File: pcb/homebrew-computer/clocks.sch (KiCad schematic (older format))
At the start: 6 parts

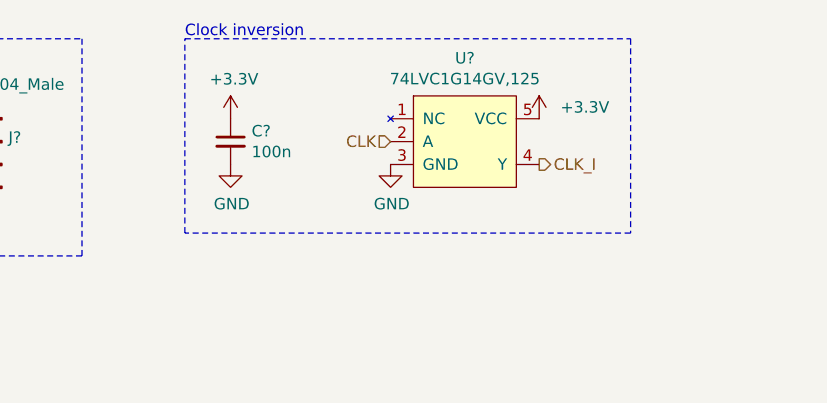
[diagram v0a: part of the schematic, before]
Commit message: Add the memory interface logic
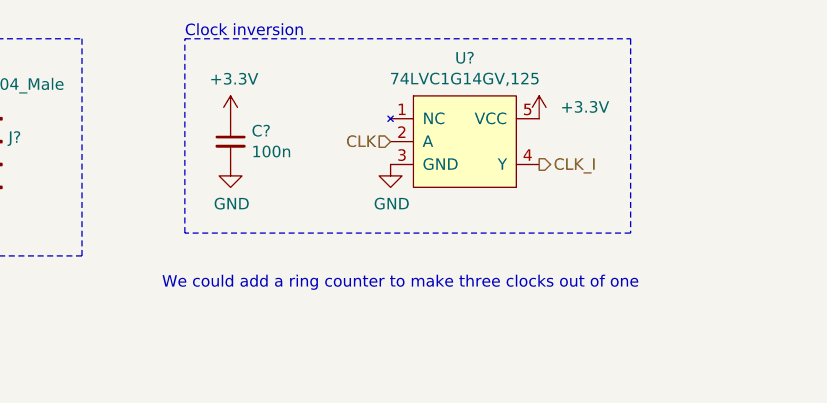
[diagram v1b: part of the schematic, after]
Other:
- note added: "We could add a ring counter to make three clocks out of one"
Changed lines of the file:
@@
 $Descr User 7874 4134
 encoding utf-8
-Sheet 7 8
+Sheet 6 8
 Title ""
 Date ""
@@
 Text Notes 4600 900  0    50   ~ 0
 Clock inversion
+Text Notes 4500 2000 0    50   ~ 0
+We could add a ring counter to make three clocks out of one
 $EndSCHEMATC

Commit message: Add beginning of peripheral ios
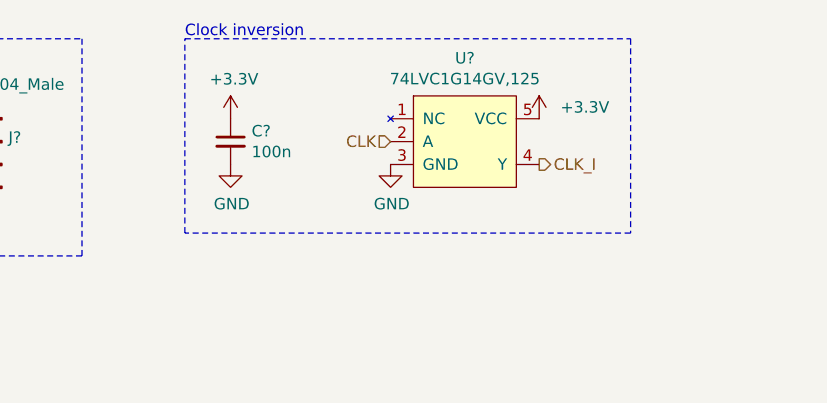
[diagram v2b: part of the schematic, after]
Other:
- note removed: "We could add a ring counter to make three clocks out of one"
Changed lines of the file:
@@
 $Descr User 7874 4134
 encoding utf-8
-Sheet 6 8
+Sheet 5 8
 Title ""
 Date ""
@@
 Text Notes 4600 900  0    50   ~ 0
 Clock inversion
-Text Notes 4500 2000 0    50   ~ 0
-We could add a ring counter to make three clocks out of one
 $EndSCHEMATC

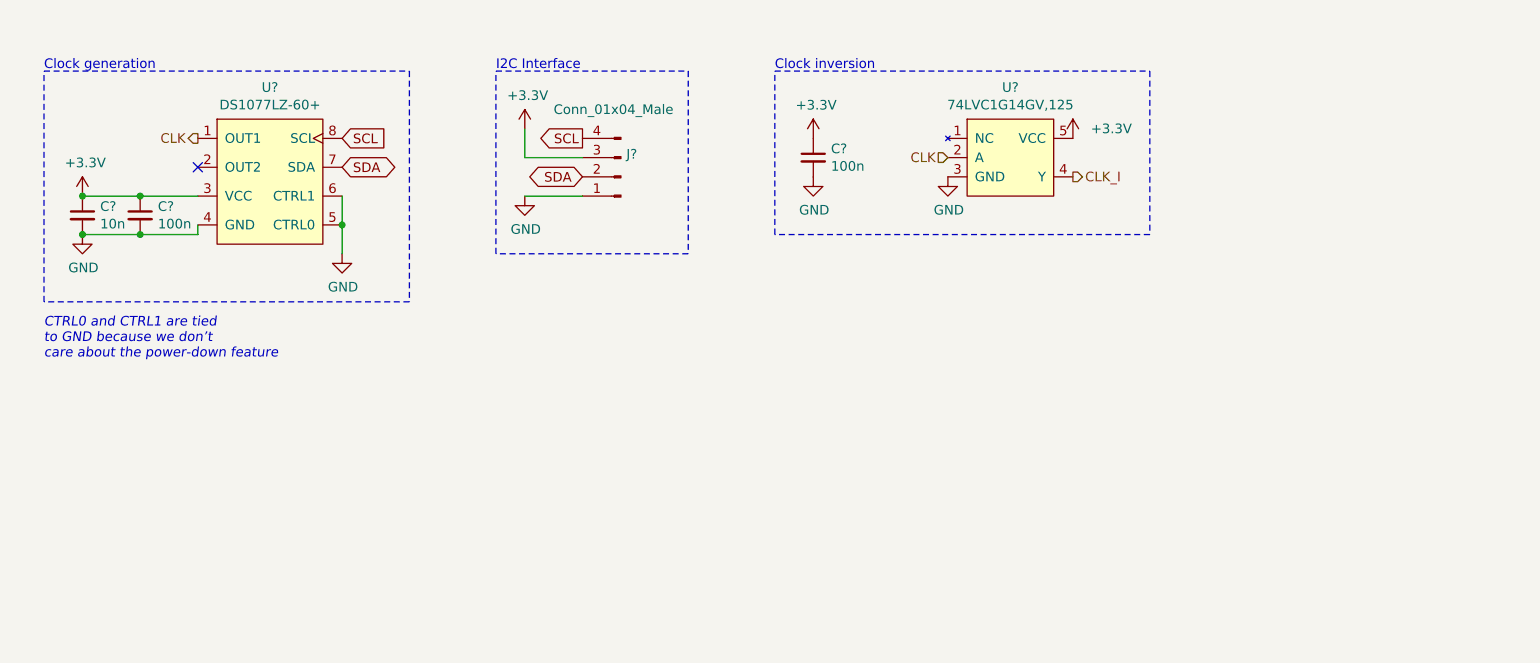
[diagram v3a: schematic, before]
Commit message: Remove the address bus as it would require too big of a connector
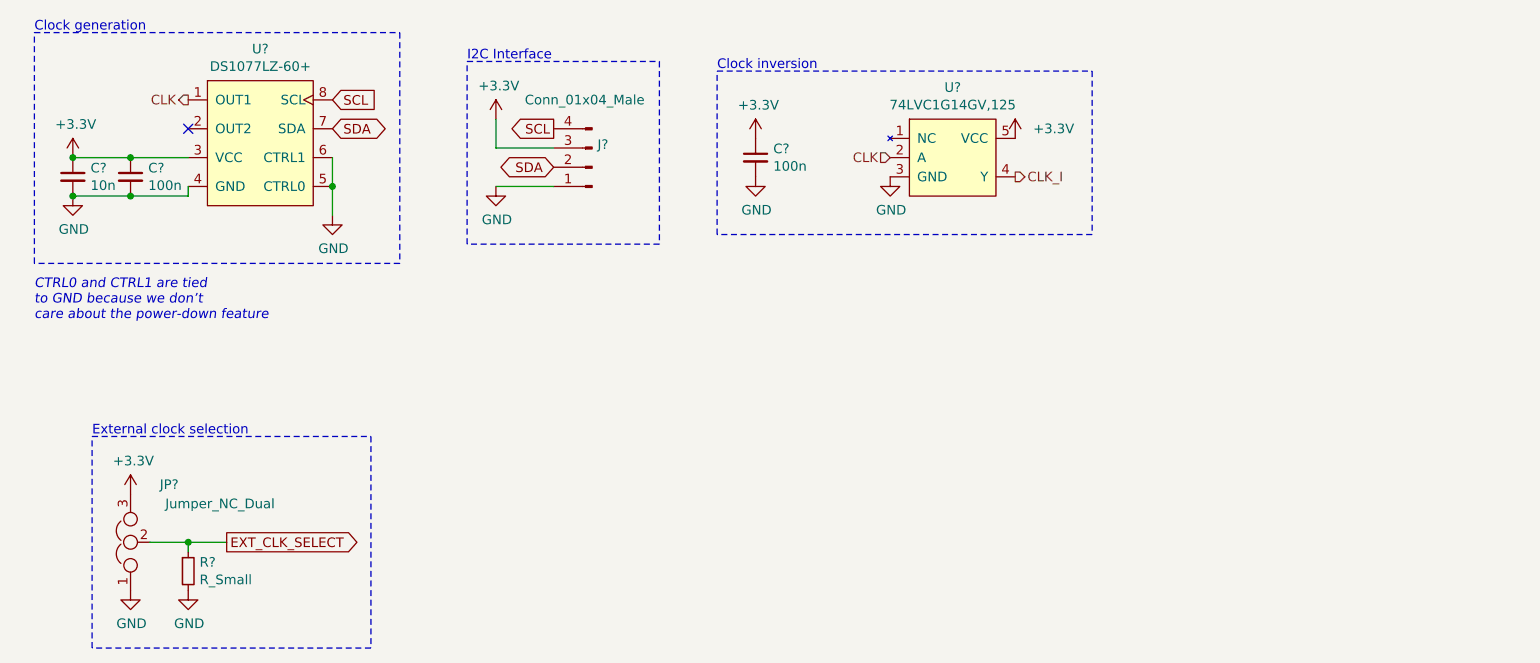
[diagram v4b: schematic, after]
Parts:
- added JP?: Jumper_NC_Dual, symbol Device:Jumper_NC_Dual
- added R?: R_Small, symbol Device:R_Small
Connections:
- net +3V3: now also JP?.3
- net GND: now also JP?.1, R?.2
- new net EXT_CLK_SELECT: JP?.2, R?.1
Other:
- note added: "External clock selection"
- moved on the sheet: C?, J?, U?

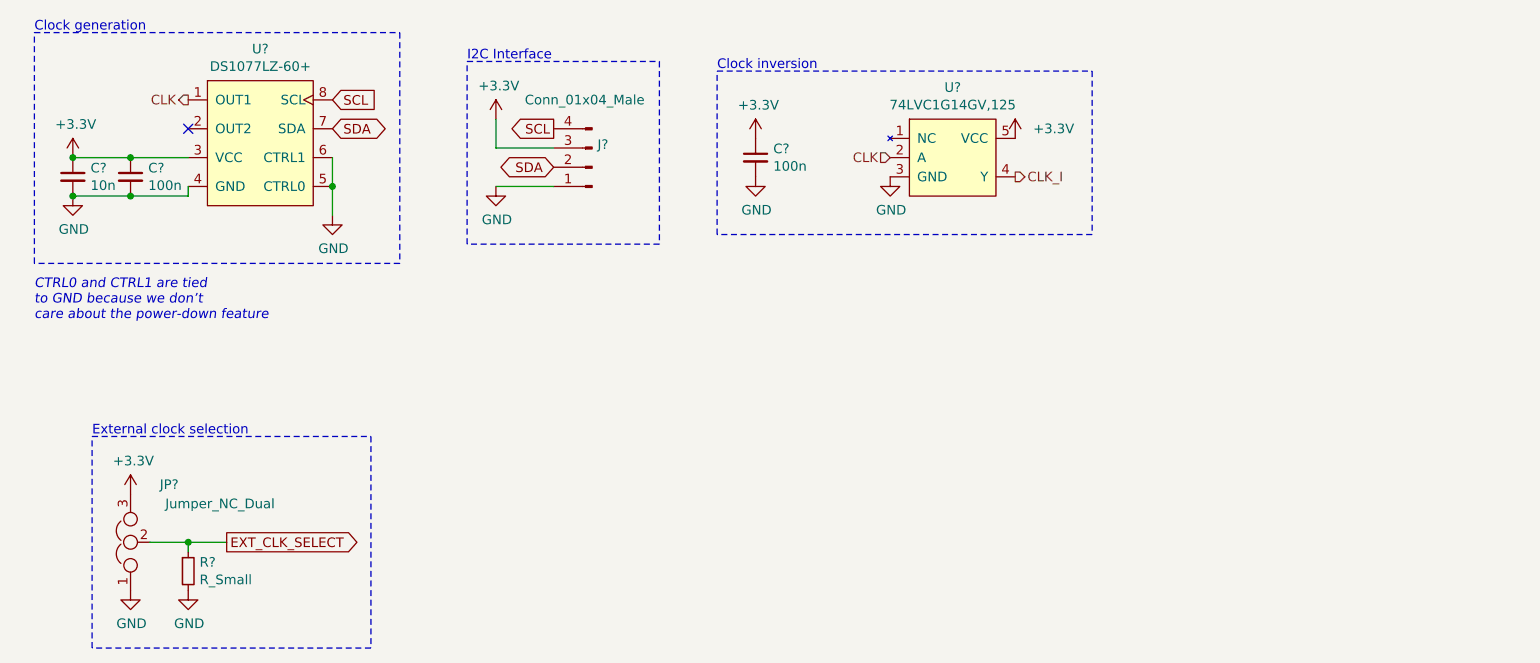
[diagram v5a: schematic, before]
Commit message: Add program counter
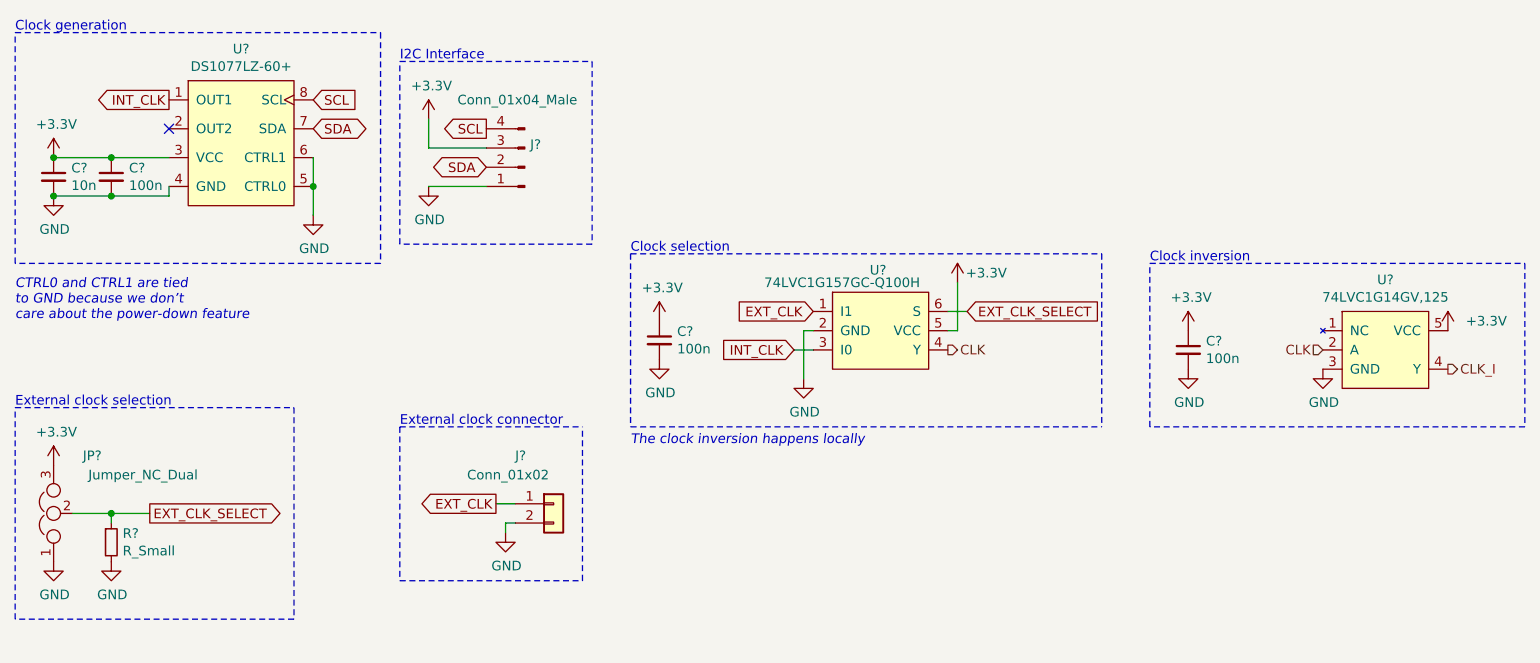
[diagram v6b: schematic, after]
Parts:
- added C?: 100n, symbol Device:C_Small
- added J?: Conn_01x02, symbol Connector_Generic:Conn_01x02
- added U?: 74LVC1G157GC-Q100H, symbol 74LVC1G157:74LVC1G157GC-Q100H
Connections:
- net +3V3: now also C?.1, U?.5 (VCC)
- net CLK: now also U?.4 (Y); no longer U?.1 (OUT1)
- net EXT_CLK_SELECT: now also U?.6 (S)
- net GND: now also C?.2, J?.2 (Pin_2), U?.2 (GND)
- new net EXT_CLK: J?.1 (Pin_1), U?.1 (I1)
- new net INT_CLK: U?.1 (OUT1), U?.3 (I0)
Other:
- note added: "Clock selection"
- note added: "External clock connector"
- note added: "The clock inversion happens locally"
- moved on the sheet: C?, J?, JP?, R?, U?

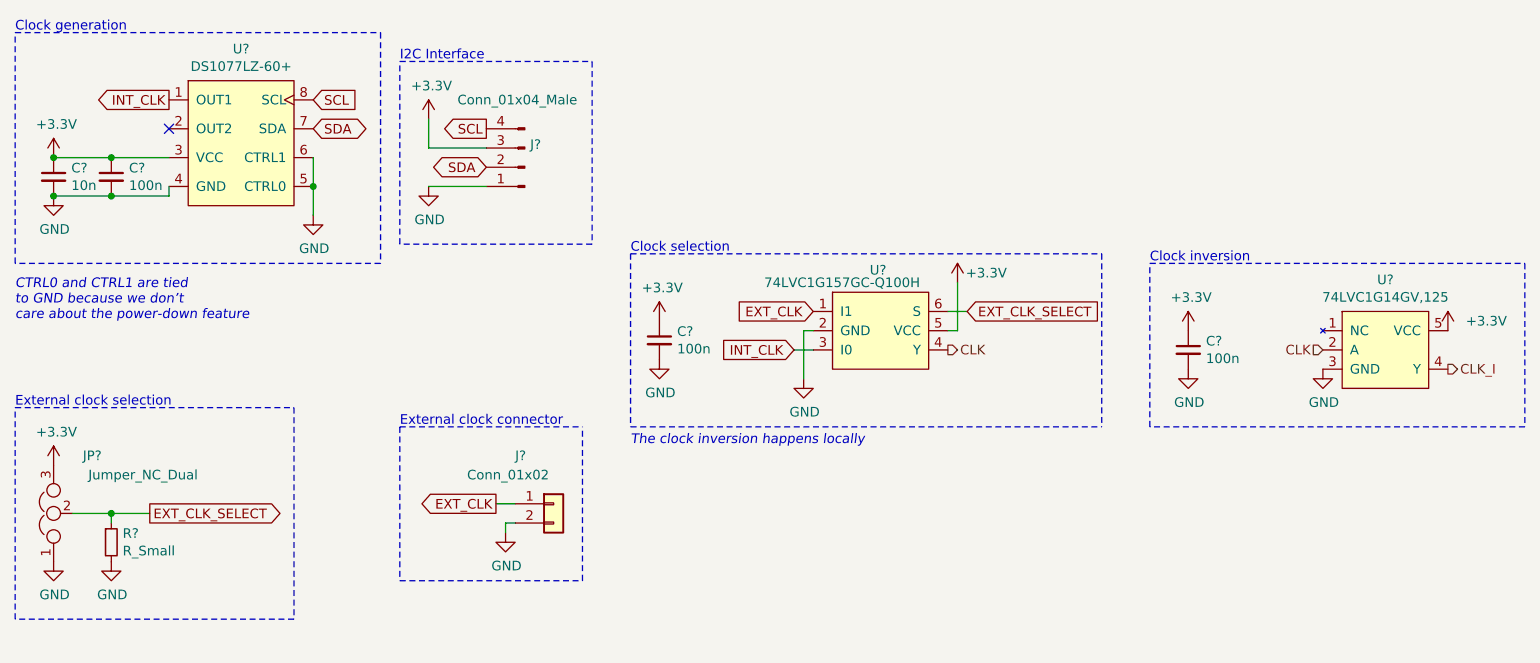
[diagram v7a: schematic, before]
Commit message: Start changing global labels with local labels
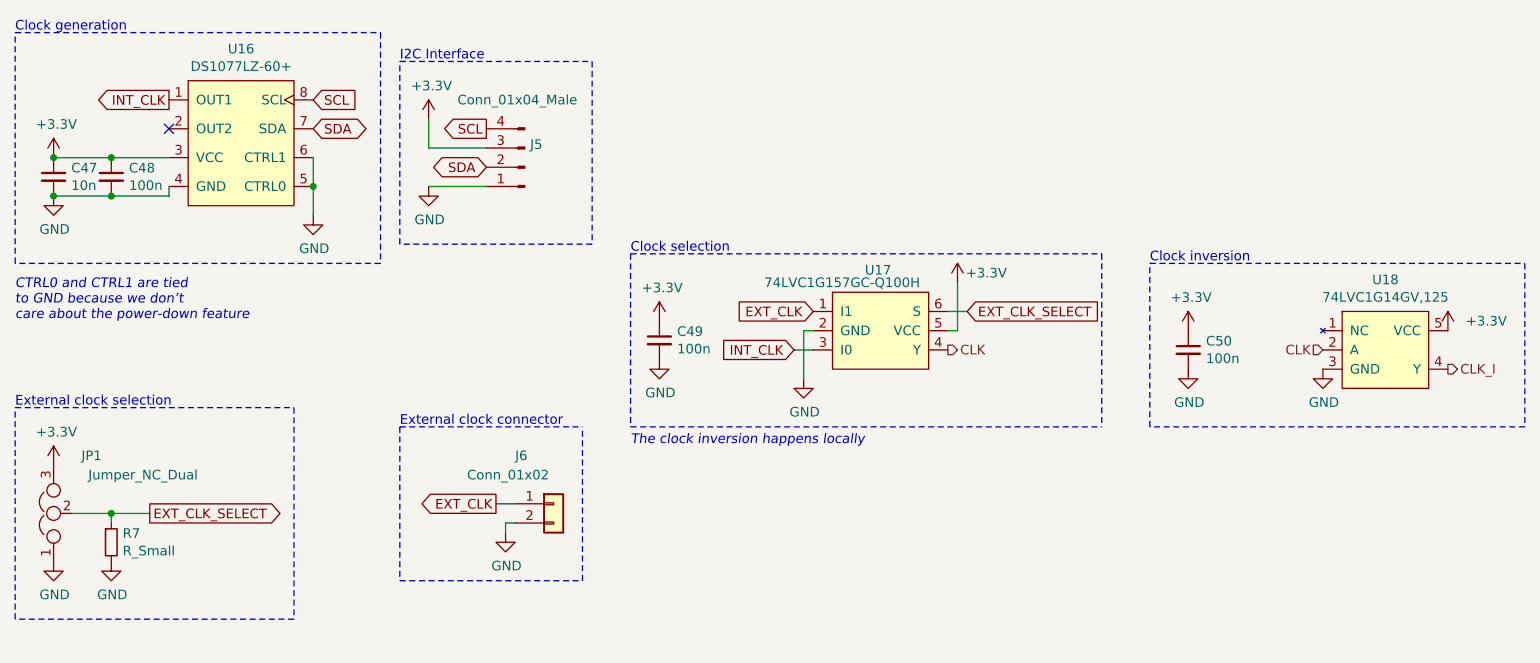
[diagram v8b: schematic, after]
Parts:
- gave numbers to parts that had none: 11
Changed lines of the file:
@@
 $EndDescr
 $Comp
-L DS1077L:DS1077LZ-60+ U?
+L DS1077L:DS1077LZ-60+ U16
 U 1 1 5F903AB7
 P 1900 800
-F 0 "U?" H 1825 815 50  0000 C CNN
+F 0 "U16" H 1825 815 50  0000 C CNN
 F 1 "DS1077LZ-60+" H 1825 724 50  0000 C CNN
 F 2 "" H 1900 800 50  0001 C CNN
@@
 $EndComp
 $Comp
-L Device:C_Small C?
+L Device:C_Small C48
 U 1 1 5F904F83
 P 1150 1450
-F 0 "C?" H 1242 1496 50  0000 L CNN
+F 0 "C48" H 1242 1496 50  0000 L CNN
 F 1 "100n" H 1242 1405 50  0000 L CNN
 F 2 "" H 1150 1450 50  0001 C CNN
@@
 $EndComp
 $Comp
-L Device:C_Small C?
+L Device:C_Small C47
 U 1 1 5F905EB9
 P 850 1450
-F 0 "C?" H 942 1496 50  0000 L CNN
+F 0 "C47" H 942 1496 50  0000 L CNN
 F 1 "10n" H 942 1405 50  0000 L CNN
 F 2 "" H 850 1450 50  0001 C CNN
@@
 CTRL0 and CTRL1 are tied\nto GND because we don’t \ncare about the power-down feature
 $Comp
-L Connector:Conn_01x04_Male J?
+L Connector:Conn_01x04_Male J5
 U 1 1 5F90DBBD
 P 3300 1400
-F 0 "J?" H 3272 1282 50  0000 R CNN
+F 0 "J5" H 3272 1282 50  0000 R CNN
 F 1 "Conn_01x04_Male" H 3650 1050 50  0000 R CNN
 F 2 "" H 3300 1400 50  0001 C CNN
@@
 I2C Interface
 $Comp
-L 74LVC1G14:74LVC1G14GV,125 U?
+L 74LVC1G14:74LVC1G14GV,125 U18
 U 1 1 5F90FC95
 P 7800 2050
-F 0 "U?" H 7775 2115 50  0000 C CNN
+F 0 "U18" H 7775 2115 50  0000 C CNN
 F 1 "74LVC1G14GV,125" H 7775 2024 50  0000 C CNN
 F 2 "" H 7800 2050 50  0001 C CNN
@@
 $EndComp
 $Comp
-L Device:C_Small C?
+L Device:C_Small C50
 U 1 1 5F910640
 P 6750 2350
-F 0 "C?" H 6842 2396 50  0000 L CNN
+F 0 "C50" H 6842 2396 50  0000 L CNN
 F 1 "100n" H 6842 2305 50  0000 L CNN
 F 2 "" H 6750 2350 50  0001 C CNN
@@
 Clock inversion
 $Comp
-L Device:Jumper_NC_Dual JP?
+L Device:Jumper_NC_Dual JP1
 U 1 1 5FB84D34
 P 850 3200
-F 0 "JP?" V 1150 2950 50  0000 L CNN
+F 0 "JP1" V 1150 2950 50  0000 L CNN
 F 1 "Jumper_NC_Dual" V 1050 2450 50  0000 L CNN
 F 2 "" H 850 3200 50  0001 C CNN
@@
 $EndComp
 $Comp
-L Device:R_Small R?
+L Device:R_Small R7
 U 1 1 5FB8BDB1
 P 1150 3350
-F 0 "R?" H 1209 3396 50  0000 L CNN
+F 0 "R7" H 1209 3396 50  0000 L CNN
 F 1 "R_Small" H 1209 3305 50  0000 L CNN
 F 2 "" H 1150 3350 50  0001 C CNN
@@
 External clock connector
 $Comp
-L 74LVC1G157:74LVC1G157GC-Q100H U?
+L 74LVC1G157:74LVC1G157GC-Q100H U17
 U 1 1 5FACB866
 P 5150 2000
-F 0 "U?" H 5137 2065 50  0000 C CNN
+F 0 "U17" H 5137 2065 50  0000 C CNN
 F 1 "74LVC1G157GC-Q100H" H 4950 2000 50  0000 C CNN
 F 2 "" H 5150 2000 50  0001 C CNN
@@
 Clock selection
 $Comp
-L Connector_Generic:Conn_01x02 J?
+L Connector_Generic:Conn_01x02 J6
 U 1 1 5FAD3D98
 P 3450 3150
-F 0 "J?" H 3250 3400 50  0000 L CNN
+F 0 "J6" H 3250 3400 50  0000 L CNN
 F 1 "Conn_01x02" H 3000 3300 50  0000 L CNN
 F 2 "" H 3450 3150 50  0001 C CNN
@@
 $EndComp
 $Comp
-L Device:C_Small C?
+L Device:C_Small C49
 U 1 1 5FAD6849
 P 4000 2300
-F 0 "C?" H 4092 2346 50  0000 L CNN
+F 0 "C49" H 4092 2346 50  0000 L CNN
 F 1 "100n" H 4092 2255 50  0000 L CNN
 F 2 "" H 4000 2300 50  0001 C CNN
